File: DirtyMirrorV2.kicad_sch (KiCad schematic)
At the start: 46 parts, among them U1 TL074, U2 TL074, U4 TL072

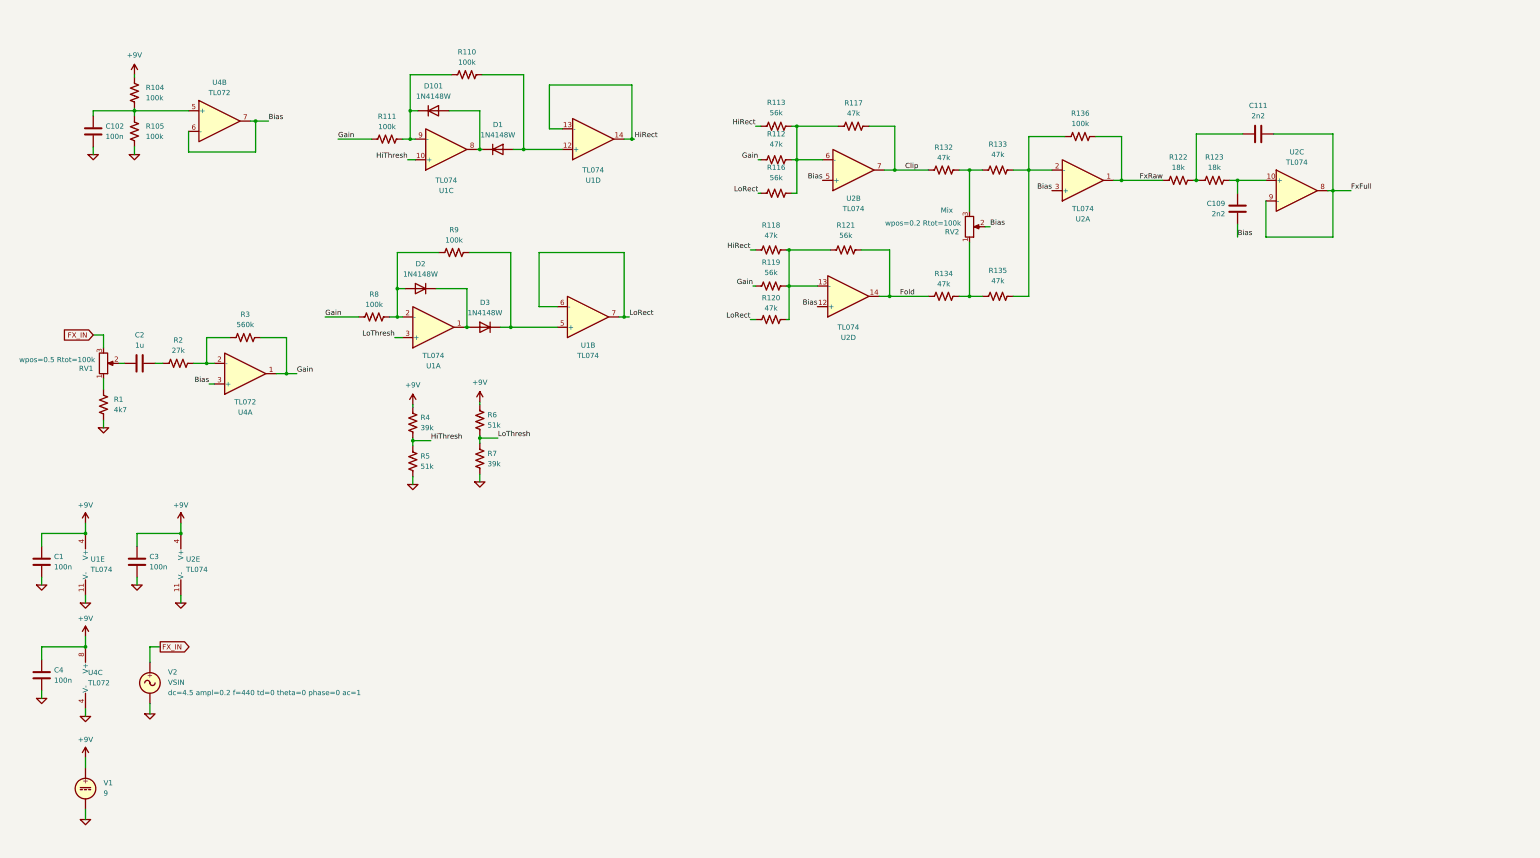
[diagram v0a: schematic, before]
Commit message: simulation working, schem labeled
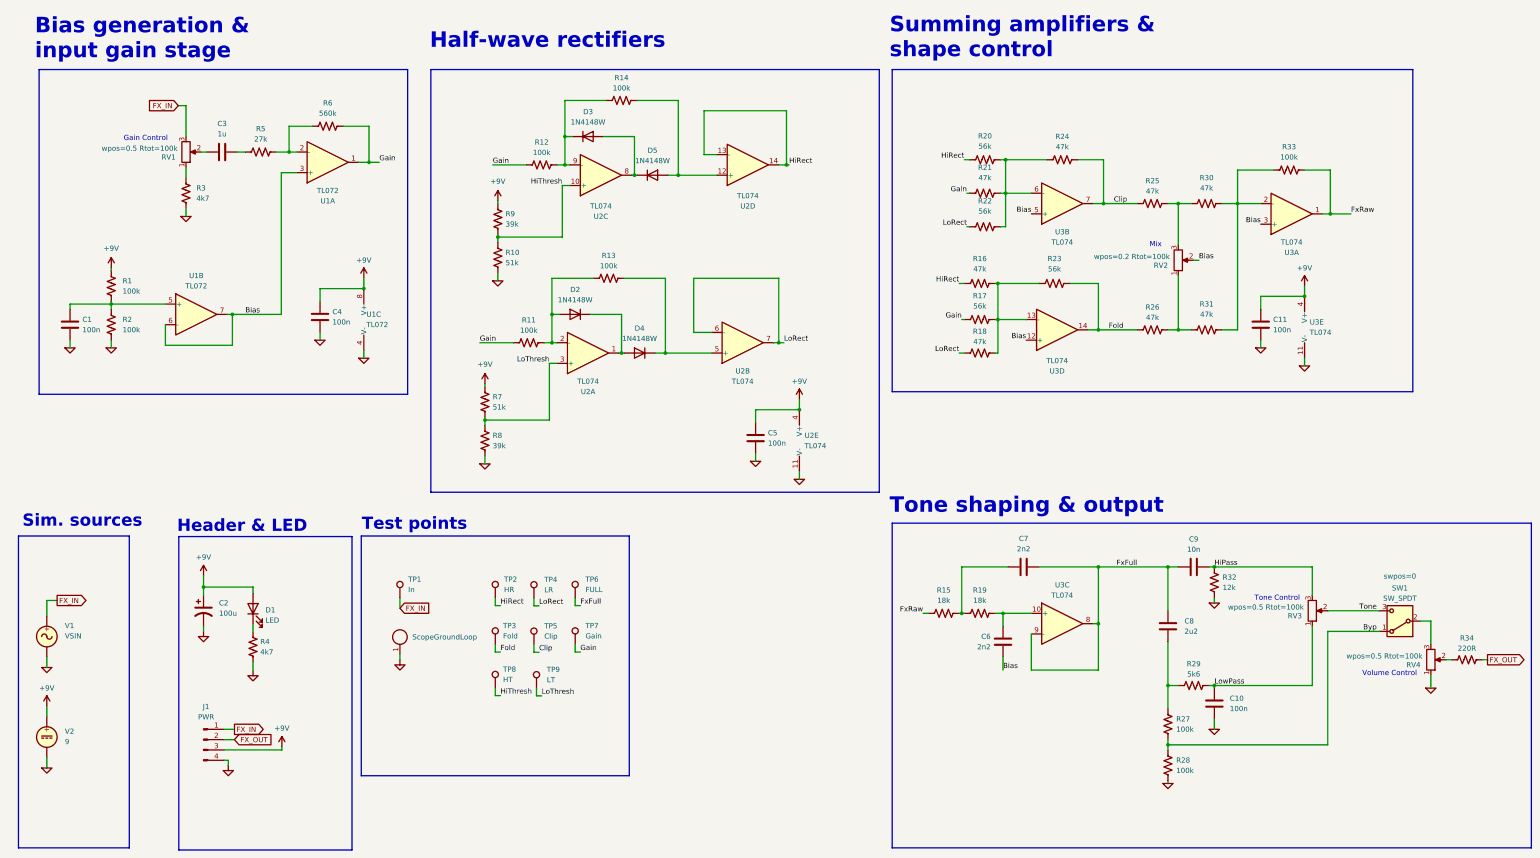
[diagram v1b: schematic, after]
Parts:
- added C10: 100n, Capacitor_SMD:C_0805_2012Metric, symbol Device:C
- added C2: 100u, Capacitor_THT:CP_Radial_D5.0mm_P2.50mm, symbol Device:C_Polarized_US
- added C8: 2u2, Capacitor_SMD:C_0805_2012Metric, symbol Device:C
- added C9: 10n, Capacitor_SMD:C_0805_2012Metric, symbol Device:C
- added D1: LED, LED_THT:LED_D3.0mm, symbol Device:LED
- added J1: PWR, Connector_PinHeader_2.54mm:PinHeader_1x04_P2.54mm_Vertical, symbol Connector:Conn_01x04_Pin
- added J2: ScopeGroundLoop, Connector:THT_GND_WIRE, symbol Connector:ScopeGroundLoop
- added R27, R28: 100k, Resistor_SMD:R_0805_2012Metric, symbol Device:R_US
- added R29: 5k6, Resistor_SMD:R_0805_2012Metric, symbol Device:R_US
- added R32: 12k, Resistor_SMD:R_0805_2012Metric, symbol Device:R_US
- added R34: 220R, Resistor_SMD:R_0805_2012Metric, symbol Device:R_US
- added R4: 4k7, Resistor_SMD:R_0805_2012Metric, symbol Device:R_US
- added RV3, RV4: R_Potentiometer, symbol Device:R_Potentiometer
- added SW1: SW_SPDT, Connector_PinSocket_2.54mm:PinSocket_1x03_P2.54mm_Vertical, symbol Switch:SW_SPDT
- added TP1: In, TestPoint:TestPoint_THTPad_D2.0mm_Drill1.0mm_VAL, symbol Connector:TestPoint
- added TP2: HR, TestPoint:TestPoint_THTPad_D2.0mm_Drill1.0mm_VAL, symbol Connector:TestPoint
- added TP3: Fold, TestPoint:TestPoint_THTPad_D2.0mm_Drill1.0mm_VAL, symbol Connector:TestPoint
- added TP4: LR, TestPoint:TestPoint_THTPad_D2.0mm_Drill1.0mm_VAL, symbol Connector:TestPoint
- added TP5: Clip, TestPoint:TestPoint_THTPad_D2.0mm_Drill1.0mm_VAL, symbol Connector:TestPoint
- added TP6: FULL, TestPoint:TestPoint_THTPad_D2.0mm_Drill1.0mm_VAL, symbol Connector:TestPoint
- added TP7: Gain, TestPoint:TestPoint_THTPad_D2.0mm_Drill1.0mm_VAL, symbol Connector:TestPoint
- added TP8: HT, TestPoint:TestPoint_THTPad_D2.0mm_Drill1.0mm_VAL, symbol Connector:TestPoint
- added TP9: LT, TestPoint:TestPoint_THTPad_D2.0mm_Drill1.0mm_VAL, symbol Connector:TestPoint
- renumbered C102 to C1, C3 to C11, C2 to C3, C1 to C5, C109 to C6, C111 to C7, D101 to D3, D3 to D4, D1 to D5, R104 to R1, R5 to R10, R8 to R11, R111 to R12, R9 to R13, R110 to R14, R122 to R15, R118 to R16, R119 to R17, R120 to R18, R123 to R19, R105 to R2, R113 to R20, R112 to R21, R116 to R22, R121 to R23, R117 to R24, R132 to R25, R134 to R26, R1 to R3, R133 to R30, R135 to R31, R136 to R33, R2 to R5, R3 to R6, R6 to R7, R7 to R8, R4 to R9, U4 to U1, U1 to U2, U2 to U3, V2 to V1, V1 to V2
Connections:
- net +9V: now also C2.1, D1.2 (A), J1.3 (Pin_3)
- net 0: now also C10.2, R28.2, R32.2, RV4.1
- net Clip: now also TP5.1
- net FX_IN: now also J1.1 (Pin_1), TP1.1
- net Fold: now also TP3.1
- net FxFull: now also C8.1, C9.1, TP6.1
- net Gain: now also TP7.1
- net HiRect: now also TP2.1
- net HiThresh: now also TP8.1
- net LoRect: now also TP4.1
- net LoThresh: now also TP9.1
- new net: D1.1 (K), R4.1
- new net: R34.1, RV4.2
- new net: RV4.3, SW1.2 (B)
- new net: C8.2, R27.1, R29.1
- new net Byp: R27.2, R28.1, SW1.1 (A)
- new net FX_OUT: J1.2 (Pin_2), R34.2
- new net GND: C2.2, J1.4 (Pin_4), J2.1, R4.2
- new net HiPass: C9.2, R32.1, RV3.3
- new net LowPass: C10.1, R29.2, RV3.1
- new net Tone: RV3.2, SW1.3 (C)
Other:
- note added: "Bias generation & input gain stage"
- note added: "Gain Control"
- note added: "Half-wave rectifiers"
- note added: "Header & LED"
- note added: "Sim. sources"
- note added: "Summing amplifiers & shape control"
- note added: "Test points"
- note added: "Tone Control"
- note added: "Tone shaping & output"
- note added: "Volume Control"
- moved on the sheet: C1, C11, C3, C4, C5, C6, C7, D2, D3, D4, D5, R1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

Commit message: footprints assigned
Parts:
- J2: footprint Connector:THT_GND_WIRE -> Connector_Pin:THT_GND_WIRE
- R5, R6: footprint (none) -> Resistor_SMD:R_0805_2012Metric
- RV1, RV2, RV3, RV4: footprint (none) -> Potentiometer_THT:Potentiometer_Alpha_RV16AF_42_Single_Long
- U1: footprint (none) -> Package_SO:SOIC-8_3.9x4.9mm_P1.27mm
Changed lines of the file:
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@@
 			)
 		)
-		(property "Footprint" ""
+		(property "Footprint" "Package_SO:SOIC-8_3.9x4.9mm_P1.27mm"
 			(at 90.17 53.34 0)
 			(effects
@@
 			)
 		)
-		(property "Footprint" ""
+		(property "Footprint" "Potentiometer_THT:Potentiometer_Alpha_RV16AF_42_Single_Long"
 			(at 361.95 175.895 0)
 			(effects
@@
 			)
 		)
-		(property "Footprint" "Connector:THT_GND_WIRE"
+		(property "Footprint" "Connector_Pin:THT_GND_WIRE"
 			(at 107.95 167.005 0)
 			(effects
@@
 			)
 		)
-		(property "Footprint" ""
+		(property "Footprint" "Potentiometer_THT:Potentiometer_Alpha_RV16AF_42_Single_Long"
 			(at 332.74 163.83 0)
 			(effects
@@
 			)
 		)
-		(property "Footprint" ""
+		(property "Footprint" "Package_SO:SOIC-8_3.9x4.9mm_P1.27mm"
 			(at 57.785 90.805 0)
 			(effects
@@
 			)
 		)
-		(property "Footprint" ""
+		(property "Footprint" "Potentiometer_THT:Potentiometer_Alpha_RV16AF_42_Single_Long"
 			(at 55.245 50.8 0)
 			(effects
@@
 			)
 		)
-		(property "Footprint" ""
+		(property "Footprint" "Potentiometer_THT:Potentiometer_Alpha_RV16AF_42_Single_Long"
 			(at 299.72 77.47 0)
 			(effects
@@
 			)
 		)
-		(property "Footprint" ""
+		(property "Footprint" "Resistor_SMD:R_0805_2012Metric"
 			(at 73.914 49.784 90)
 			(effects
@@
 			)
 		)
-		(property "Footprint" ""
+		(property "Footprint" "Resistor_SMD:R_0805_2012Metric"
 			(at 90.424 43.434 90)
 			(effects
@@
 			)
 		)
-		(property "Footprint" ""
+		(property "Footprint" "Package_SO:SOIC-8_3.9x4.9mm_P1.27mm"
 			(at 101.6 92.075 0)
 			(effects

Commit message: board routed, DRC passing
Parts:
- added TP10: Out, TestPoint:TestPoint_THTPad_D2.0mm_Drill1.0mm_VAL, symbol Connector:TestPoint
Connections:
- net GND is gone; now on net 0: C2.2, J1.4 (Pin_4), J2.1, R4.2
- net Bias: now also U3.10 (+); no longer U3.3 (+)
- net Clip: now also U3.8; no longer U3.7
- net FX_OUT: now also TP10.1
- net Fold: now also U3.7; no longer U3.14
- net FxFull: now also U3.1, U3.2 (-); no longer U3.8, U3.9 (-)
- net FxRaw: now also U3.14; no longer U3.1
- net HiRect: now also U2.1, U2.2 (-); no longer U2.13 (-), U2.14
- net HiThresh: now also U2.12 (+); no longer U2.10 (+)
- net LoThresh: now also U2.10 (+); no longer U2.3 (+)
- net at R20.2, R21.2, R22.2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: now also U3.9 (-); no longer U3.6 (-)
- net at R16.2, R17.2, R18.2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: now also U3.6 (-); no longer U3.13 (-)
- net at D2.1 (K), D4.2 (A): now also U2.8; no longer U2.1
- net at R30.2, R31.2, R33.1: now also U3.13 (-); no longer U3.2 (-)
- net at D3.2 (A), D5.1 (K): now also U2.14; no longer U2.8
- net at D5.2 (A), R14.2: now also U2.3 (+); no longer U2.12 (+)
- net at D3.1 (K), R12.2, R14.1: now also U2.13 (-); no longer U2.9 (-)
- net at D2.2 (A), R11.2, R13.1: now also U2.9 (-); no longer U2.2 (-)
- net at C6.1, R19.2: now also U3.3 (+); no longer U3.10 (+)
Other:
- moved on the sheet: U2A, U2C, U2D, U3A, U3B, U3C, U3D

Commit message: value tweaks, added BOM
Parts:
- R24: value 47k -> 33k
- R33: value 100k -> 470k
- R4: value 4k7 -> 6k8
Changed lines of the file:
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@@
 		(fields_autoplaced yes)
 		(property "Reference" "R4"
-			(at 73.533 171.4499 0)
+			(at 73.66 171.4499 0)
 			(effects
 				(font
@@
 			)
 		)
-		(property "Value" "4k7"
-			(at 73.533 173.9899 0)
+		(property "Value" "6k8"
+			(at 73.66 173.9899 0)
 			(effects
 				(font
@@
 			)
 		)
-		(property "Value" "100k"
+		(property "Value" "470k"
 			(at 327.025 52.07 90)
 			(effects
@@
 			)
 		)
-		(property "Value" "47k"
+		(property "Value" "33k"
 			(at 271.145 49.53 90)
 			(effects

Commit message: minor tweaks after sound testing
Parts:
- R23: value 56k -> 100k
- R24: value 33k -> 82k
- R27: value 100k -> 56k
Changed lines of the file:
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@@
 		(fields_autoplaced yes)
 		(property "Reference" "R27"
-			(at 299.212 190.4999 0)
+			(at 299.72 190.4999 0)
 			(effects
 				(font
@@
 			)
 		)
-		(property "Value" "100k"
-			(at 299.212 193.0399 0)
+		(property "Value" "56k"
+			(at 299.72 193.0399 0)
 			(effects
 				(font
@@
 			)
 		)
-		(property "Sim.Params" "wpos=0.2 Rtot=100k"
+		(property "Sim.Params" "wpos=0.2 Rtot=10k"
 			(at 288.29 76.581 0)
 			(effects
@@
 		(fields_autoplaced yes)
 		(property "Reference" "R23"
-			(at 269.24 77.089 90)
+			(at 269.24 77.47 90)
 			(effects
 				(font
@@
 			)
 		)
-		(property "Value" "56k"
-			(at 269.24 79.629 90)
+		(property "Value" "100k"
+			(at 269.24 80.01 90)
 			(effects
 				(font
@@
 			)
 		)
-		(property "Value" "33k"
+		(property "Value" "82k"
 			(at 271.145 49.53 90)
 			(effects

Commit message: resistor values tweaked to taste
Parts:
- R15, R19: value 18k -> 12k
- R16, R18: value 47k -> 39k
- R27: value 56k -> 47k
- R3: value 4k7 -> 22k
- R5: value 27k -> 33k
- R6: value 560k -> 1M
- R8, R9: value 39k -> 47k

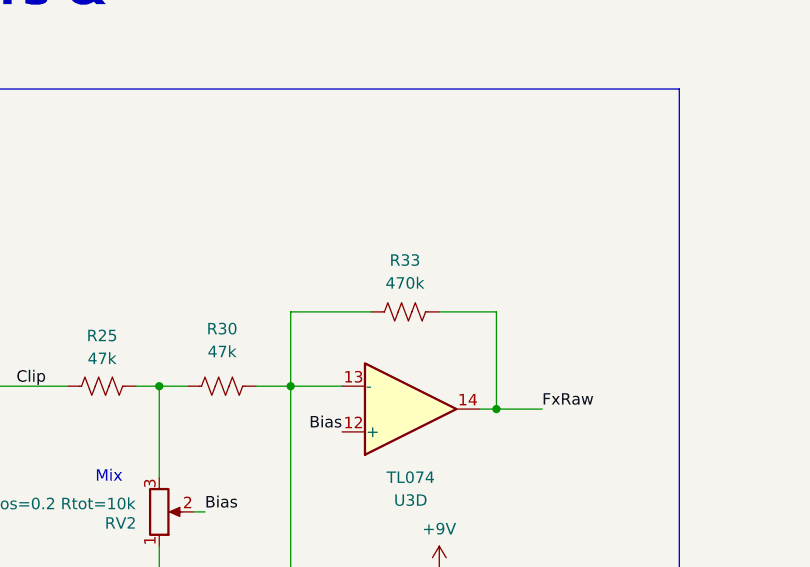
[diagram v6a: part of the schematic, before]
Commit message: higher output gain
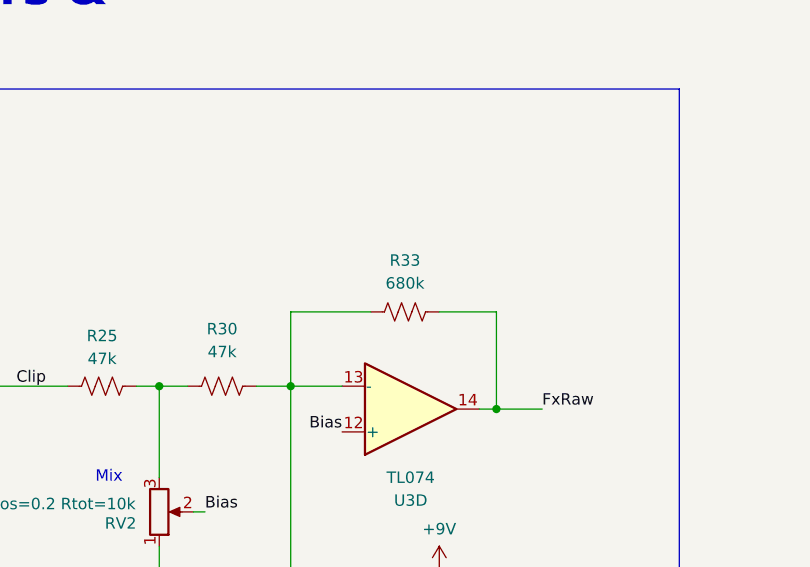
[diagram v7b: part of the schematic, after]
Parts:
- R33: value 470k -> 680k
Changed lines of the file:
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@@
 			)
 		)
-		(property "Value" "470k"
+		(property "Value" "680k"
 			(at 327.025 52.07 90)
 			(show_name no)

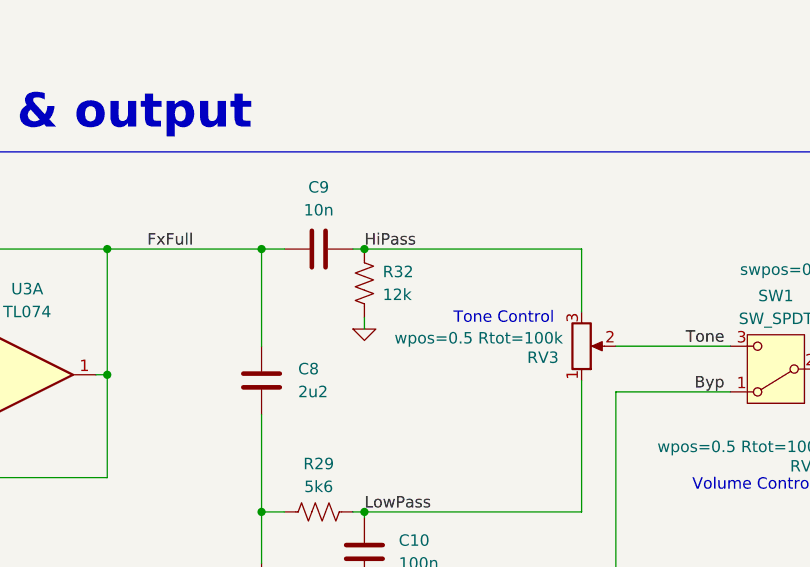
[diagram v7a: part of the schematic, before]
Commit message: changed tone ctrl high pass
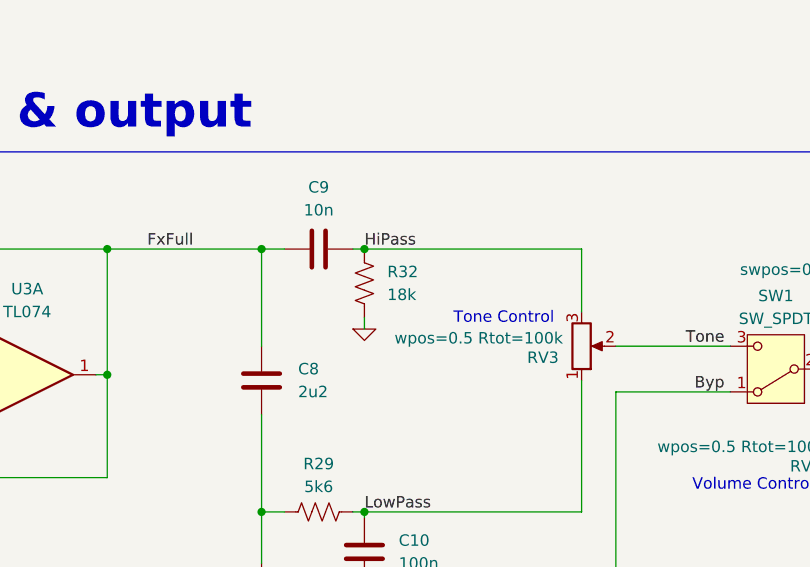
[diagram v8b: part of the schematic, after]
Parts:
- R32: value 12k -> 18k
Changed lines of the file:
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@@
 		(fields_autoplaced yes)
 		(property "Reference" "R32"
-			(at 310.642 155.5749 0)
+			(at 311.15 155.5749 0)
 			(show_name no)
 			(do_not_autoplace no)
@@
 			)
 		)
-		(property "Value" "12k"
-			(at 310.642 158.1149 0)
+		(property "Value" "18k"
+			(at 311.15 158.1149 0)
 			(show_name no)
 			(do_not_autoplace no)
